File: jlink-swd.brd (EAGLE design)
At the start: 2 parts

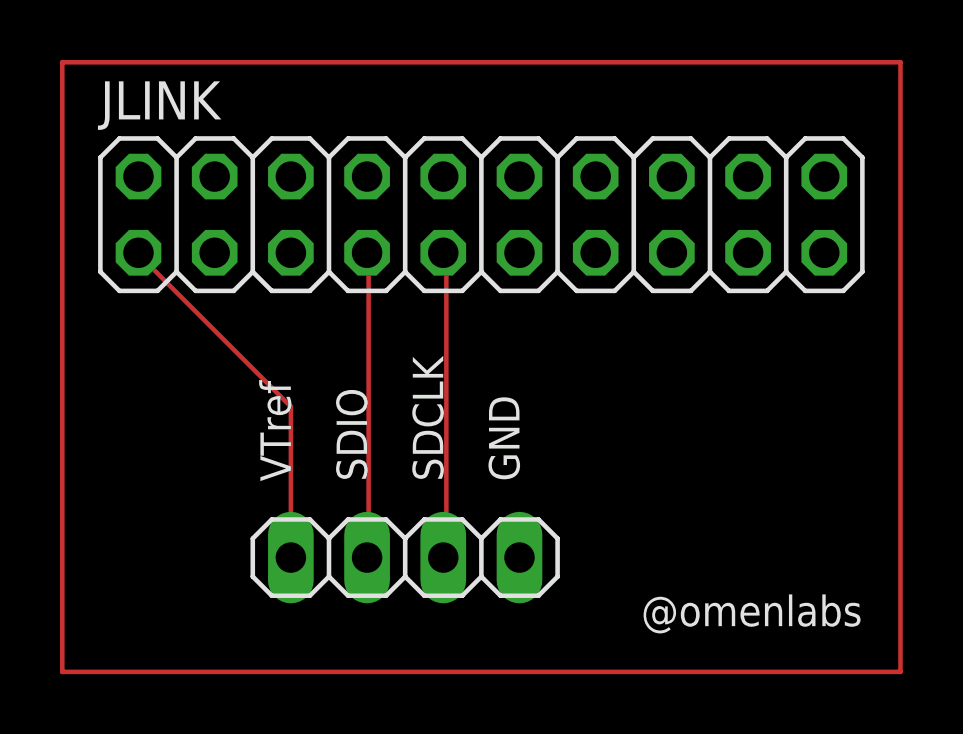
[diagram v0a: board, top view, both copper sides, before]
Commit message: Update the outline, gitignore
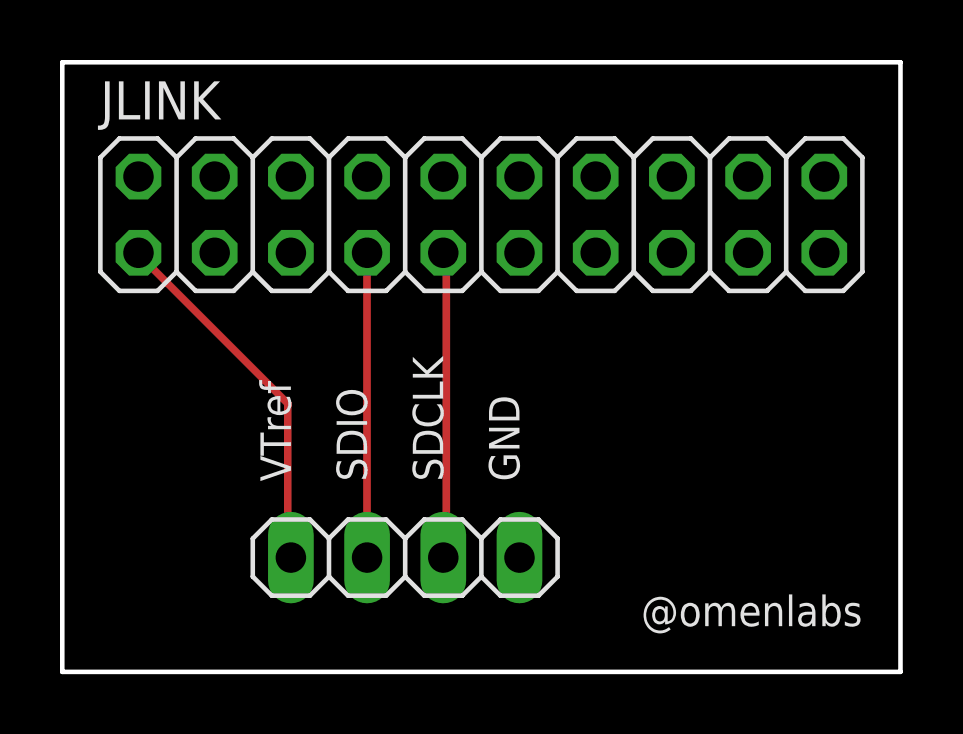
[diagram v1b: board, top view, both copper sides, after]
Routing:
- net N$1: track 96.5 -> 0.00 mm
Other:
- board outline added: 27.9 x 20.3 mm
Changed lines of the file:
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@@
 <layers>
 <layer number="1" name="Top" color="4" fill="1" visible="yes" active="yes"/>
-<layer number="16" name="Bottom" color="1" fill="1" visible="yes" active="yes"/>
-<layer number="17" name="Pads" color="2" fill="1" visible="yes" active="yes"/>
-<layer number="18" name="Vias" color="2" fill="1" visible="yes" active="yes"/>
-<layer number="19" name="Unrouted" color="6" fill="1" visible="yes" active="yes"/>
+<layer number="16" name="Bottom" color="1" fill="1" visible="no" active="yes"/>
+<layer number="17" name="Pads" color="2" fill="1" visible="no" active="yes"/>
+<layer number="18" name="Vias" color="2" fill="1" visible="no" active="yes"/>
+<layer number="19" name="Unrouted" color="6" fill="1" visible="no" active="yes"/>
 <layer number="20" name="Dimension" color="24" fill="1" visible="yes" active="yes"/>
 <layer number="21" name="tPlace" color="7" fill="1" visible="yes" active="yes"/>
@@
 <text x="12.7" y="6.35" size="1.016" layer="21" font="vector" rot="R90">SDCLK</text>
 <text x="15.24" y="6.35" size="1.016" layer="21" font="vector" rot="R90">GND</text>
+<wire x1="0" y1="0" x2="0" y2="20.32" width="0.1524" layer="20"/>
+<wire x1="0" y1="20.32" x2="27.94" y2="20.32" width="0.1524" layer="20"/>
+<wire x1="27.94" y1="20.32" x2="27.94" y2="0" width="0.1524" layer="20"/>
+<wire x1="27.94" y1="0" x2="0" y2="0" width="0.1524" layer="20"/>
 </plain>
 <attributes>
@@
 </class>
 </classes>
-<designrules name="default">
-<description language="de">&lt;b&gt;EAGLE Design Rules&lt;/b&gt;
-&lt;p&gt;
-Die Standard-Design-Rules sind so gewählt, dass sie für
-die meisten Anwendungen passen. Sollte ihre Platine
-besondere Anforderungen haben, treffen Sie die erforderlichen
-Einstellungen hier und speichern die Design Rules unter
-einem neuen Namen ab.</description>
-<description language="en">&lt;b&gt;EAGLE Design Rules&lt;/b&gt;
-&lt;p&gt;
-The default Design Rules have been set to cover
-a wide range of applications. Your particular design
-may have different requirements, so please make the
-necessary adjustments and save your customized
-design rules under a new name.</description>
+<designrules name="oshpark-2layer">
+<description language="en"></description>
 <param name="layerSetup" value="(1*16)"/>
 <param name="mtCopper" value="0.035mm 0.035mm 0.035mm 0.035mm 0.035mm 0.035mm 0.035mm 0.035mm 0.035mm 0.035mm 0.035mm 0.035mm 0.035mm 0.035mm 0.035mm 0.035mm"/>
@@
 <param name="checkValues" value="0"/>
 <param name="useDiameter" value="13"/>
-<param name="maxErrors" value="50"/>
+<param name="maxErrors" value="999999"/>
 </designrules>
 <autorouter>
@@
 <contactref element="SWD" pad="1"/>
 <wire x1="2.5908" y1="13.8684" x2="2.54" y2="13.97" width="0.1524" layer="16"/>
-<wire x1="7.62" y1="8.8392" x2="7.62" y2="3.81" width="0.1524" layer="1"/>
-<wire x1="2.5908" y1="13.8684" x2="7.62" y2="8.8392" width="0.1524" layer="1"/>
 <wire x1="2.5908" y1="13.8684" x2="2.54" y2="13.97" width="0.1524" layer="1"/>
+<wire x1="7.5184" y1="8.9408" x2="7.5184" y2="3.8608" width="0.254" layer="1"/>
+<wire x1="2.6416" y1="13.8176" x2="7.5184" y2="8.9408" width="0.254" layer="1"/>
+<wire x1="7.5184" y1="3.8608" x2="7.62" y2="3.81" width="0.254" layer="1"/>
+<wire x1="2.6416" y1="13.8176" x2="2.54" y2="13.97" width="0.254" layer="1"/>
 </signal>
 <signal name="SWDIO">
@@
 <wire x1="10.2108" y1="3.81" x2="10.16" y2="3.81" width="0.1524" layer="16"/>
 <wire x1="10.2108" y1="13.8684" x2="10.16" y2="13.97" width="0.1524" layer="16"/>
-<wire x1="10.2108" y1="13.8684" x2="10.2108" y2="3.81" width="0.1524" layer="1"/>
 <wire x1="10.2108" y1="3.81" x2="10.16" y2="3.81" width="0.1524" layer="1"/>
 <wire x1="10.2108" y1="13.8684" x2="10.16" y2="13.97" width="0.1524" layer="1"/>
+<wire x1="10.16" y1="13.97" x2="10.16" y2="3.81" width="0.254" layer="1"/>
 </signal>
 <signal name="SWCLK">
@@
 <wire x1="12.8016" y1="3.81" x2="12.7" y2="3.81" width="0.1524" layer="16"/>
 <wire x1="12.8016" y1="13.8684" x2="12.7" y2="13.97" width="0.1524" layer="16"/>
-<wire x1="12.8016" y1="13.8684" x2="12.8016" y2="3.81" width="0.1524" layer="1"/>
 <wire x1="12.8016" y1="3.81" x2="12.7" y2="3.81" width="0.1524" layer="1"/>
 <wire x1="12.8016" y1="13.8684" x2="12.7" y2="13.97" width="0.1524" layer="1"/>
+<wire x1="12.8016" y1="13.8176" x2="12.8016" y2="3.8608" width="0.254" layer="1"/>
+<wire x1="12.8016" y1="3.8608" x2="12.7" y2="3.81" width="0.254" layer="1"/>
+<wire x1="12.8016" y1="13.8176" x2="12.7" y2="13.97" width="0.254" layer="1"/>
 </signal>
 <signal name="GND">
@@
 </polygon>
 </signal>
-<signal name="N$1">
-<wire x1="0" y1="20.32" x2="27.94" y2="20.32" width="0.1524" layer="1"/>
-<wire x1="27.94" y1="20.32" x2="27.94" y2="0" width="0.1524" layer="1"/>
-<wire x1="27.94" y1="0" x2="0" y2="0" width="0.1524" layer="1"/>
-<wire x1="0" y1="20.32" x2="0" y2="0" width="0.1524" layer="1"/>
-</signal>
 </signals>
